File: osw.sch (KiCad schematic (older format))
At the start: 65 parts, among them J1 Conn_01x02, Q1 2N7002, SW1 SW_Push, SW2 SW_Push, SW4 SW_Push, SW5 SW_Push, U1 DS3231MZ, U10 XC6209, U11 MCP73831T-2ACI_OT, U12 USBLC6-2SC6, U13 XC6209, U2 BMA400, U3 BMP280, U4 GC9A01_IPS_display, U5 USB-OTG, U6 CH340E, U7 ttgo-32-micro, U8 Quectel_L96, U9 TPS2115A

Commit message: finalize rev 3.0
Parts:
- removed U12: USBLC6-2SC6, Package_TO_SOT_SMD:SOT-23-6, symbol Power_Protection:USBLC6-2SC6
- removed U3: BMP280, open-Smartwatch:Bosch_LGA-8_2x2.5mm_P0.65mm_ClockwisePinNumbering, symbol open-Smartwatch:BMP280
- added R23: 56k, Resistor_SMD:R_0603_1608Metric, symbol Device:R_Small
- added R24, R25: 1k, Resistor_SMD:R_0603_1608Metric, symbol Device:R_Small
- added R26: 10k, Resistor_SMD:R_0603_1608Metric, symbol Device:R_Small
- added U3: PSRAM64H, Package_SO:SOP-8_3.9x4.9mm_P1.27mm, symbol open-Smartwatch:PSRAM64H
- R16: value 1M -> 200k
- R17: value 220k -> 10k
- R19: value 2.2K -> 200k
- R20: value 2.2K -> 10k
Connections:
- net labels added: 3DFIX_2V8, 3DFIX_3V3, CLK, D_N, D_P, GEO_F2V8, GEO_F3V3, GPIO10, GPS_FON2V8, GPS_FON3V3, SD0, SD1, SD2, SD3
- net labels removed: D1_N, D1_P, D2_N, D2_P, PWR2_EN
- wire segments 357 -> 369
- no-connect marks 30 -> 18
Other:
- note added: "LEVEL SHIFTERS"
- note added: "PSRAM"
- note removed: "GPS_FON"
- note removed: "I2C addr\n0x76"
- moved on the sheet: J1, R12, R2, R3

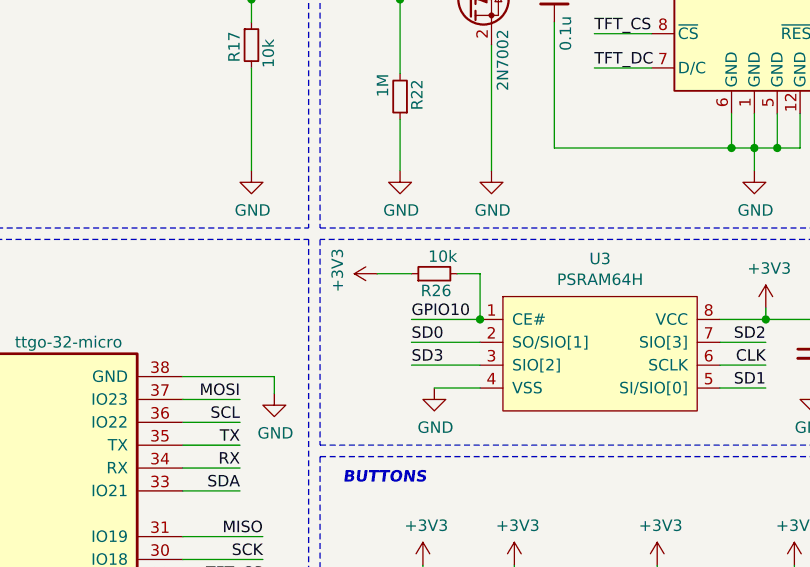
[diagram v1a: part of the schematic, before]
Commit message: rev 3.1 - remove pull up - fix ttgo32 footprint
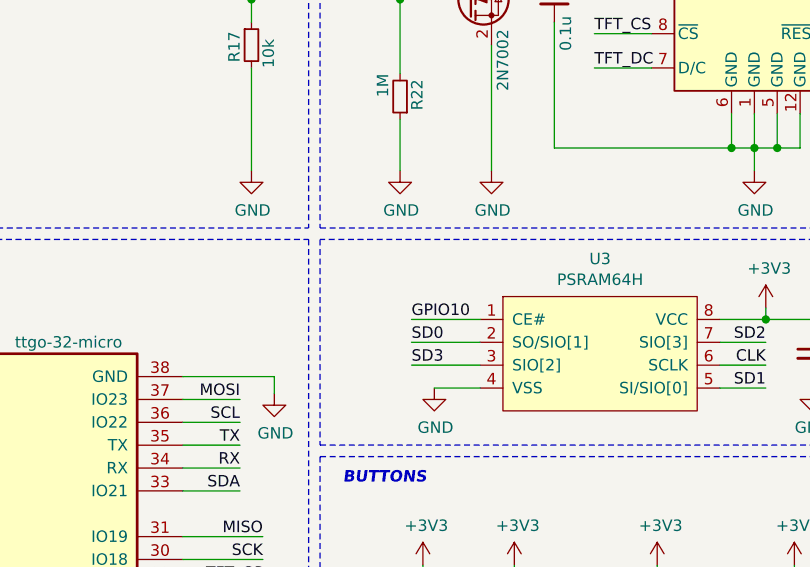
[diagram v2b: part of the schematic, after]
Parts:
- removed R26: 10k, Resistor_SMD:R_0603_1608Metric, symbol Device:R_Small
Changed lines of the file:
@@
 Sheet 1 1
 Title "Open-Smartwatch-GPS"
-Date "2021-01-26"
-Rev "3.0"
+Date "2021-02-18"
+Rev "3.1"
 Comp ""
 Comment1 ""
@@
 Wire Wire Line
 	7600 2850 7400 2850
-$Comp
-L power:+3V3 #PWR0104
-U 1 1 608696F2
-P 5900 2650
-F 0 "#PWR0104" H 5900 2500 50  0001 C CNN
-F 1 "+3V3" H 5915 2823 50  0000 C CNN
-F 2 "" H 5900 2650 50  0001 C CNN
-F 3 "" H 5900 2650 50  0001 C CNN
-	1    5900 2650
-	0    -1   -1   0
-$EndComp
-$Comp
-L Device:R_Small R26
-U 1 1 60869F0B
-P 6150 2650
-F 0 "R26" V 6075 2575 50  0000 L CNN
-F 1 "10k" V 6225 2550 50  0000 L CNN
-F 2 "Resistor_SMD:R_0603_1608Metric" H 6150 2650 50  0001 C CNN
-F 3 "~" H 6150 2650 50  0001 C CNN
-	1    6150 2650
-	0    -1   -1   0
-$EndComp
-Wire Wire Line
-	6250 2650 6350 2650
-Wire Wire Line
-	6350 2650 6350 2850
-Connection ~ 6350 2850
-Wire Wire Line
-	5900 2650 6050 2650
 Text Label 3850 5350 0    50   ~ 0
 GPIO10
